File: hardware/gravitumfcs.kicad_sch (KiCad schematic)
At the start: 0 parts

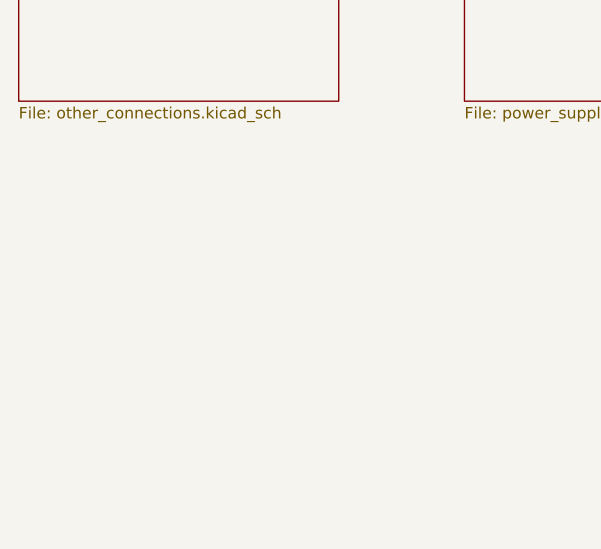
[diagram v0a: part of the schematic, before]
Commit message: schematic and BOM done
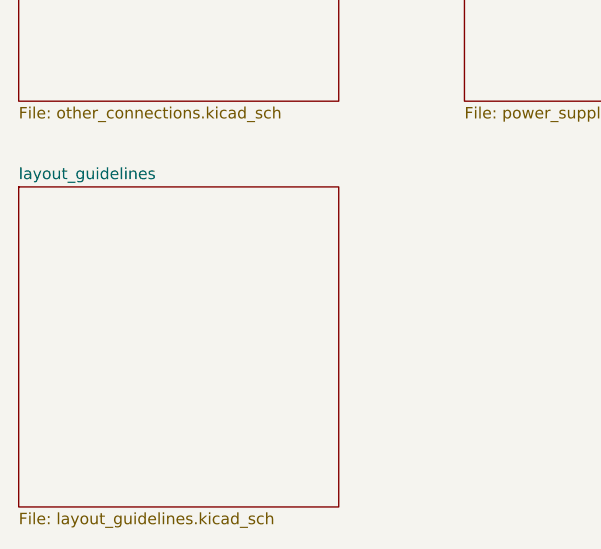
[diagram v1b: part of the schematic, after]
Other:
- added sheet layout_guidelines (layout_guidelines.kicad_sch)
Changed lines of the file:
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@@
+	)
+	(sheet
+		(at 71.12 137.795)
+		(size 35.56 35.56)
+		(exclude_from_sim no)
+		(in_bom yes)
+		(on_board yes)
+		(dnp no)
+		(fields_autoplaced yes)
+		(stroke
+			(width 0.1524)
+			(type solid)
+		)
+		(fill
+			(color 0 0 0 0.0000)
+		)
+		(property "Sheetname" "layout_guidelines"
+			(at 71.12 137.0834 0)
+			(effects
+				(font
+					(size 1.27 1.27)
+				)
+				(justify left bottom)
+			)
+		)
+		(property "Sheetfile" "layout_guidelines.kicad_sch"
+			(at 71.12 173.9396 0)
+			(effects
+				(font
+					(size 1.27 1.27)
+				)
+				(justify left top)
+			)
+		)
+		(instances
+			(project "gravitumfcs"
+				(path "/7dce3647-2289-405b-b84a-b8061fb27a64"
+					(page "8")
+				)
+			)
+		)
 	)
 	(sheet
